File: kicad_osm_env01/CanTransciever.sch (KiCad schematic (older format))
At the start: 23 parts, among them U8 SN65HVD230

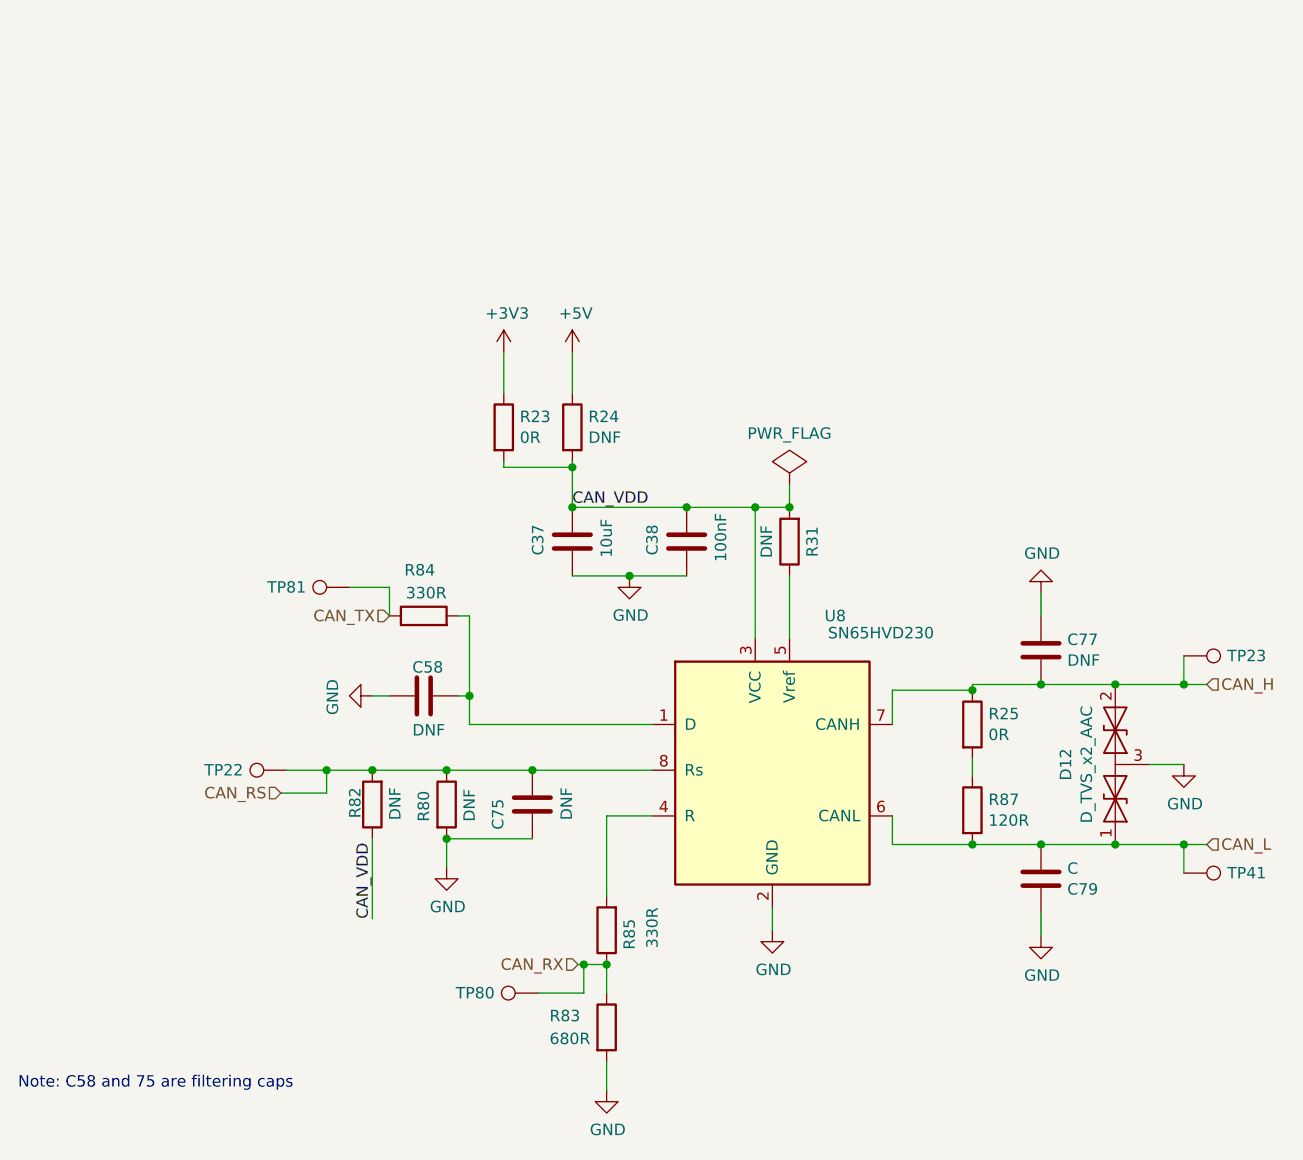
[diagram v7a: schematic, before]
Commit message: updated schematics
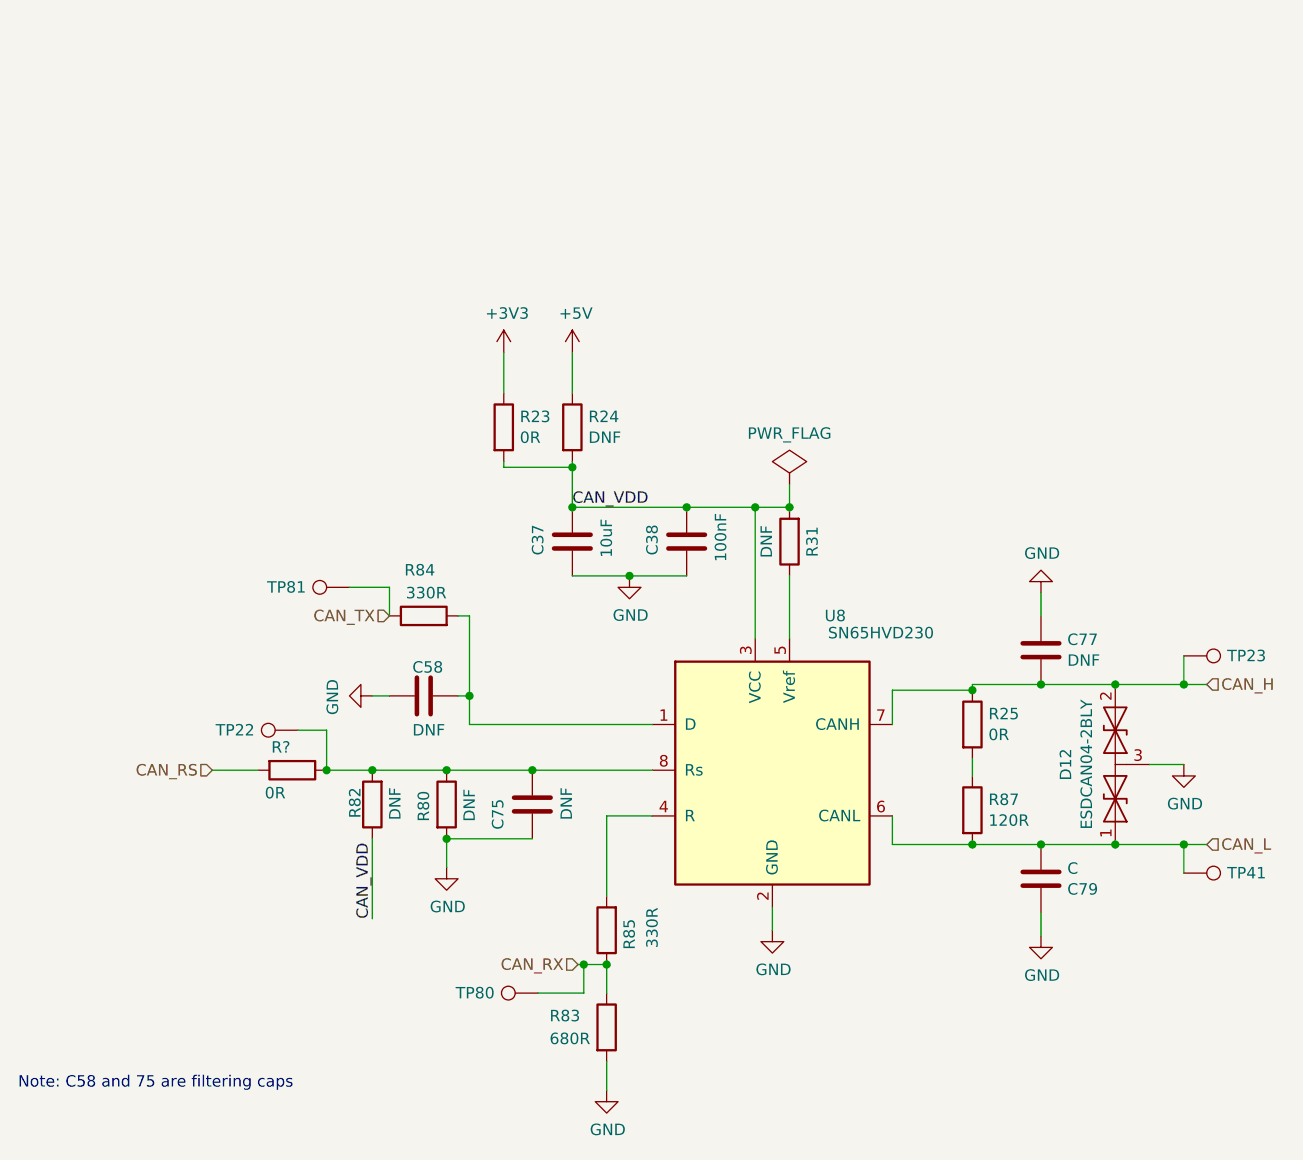
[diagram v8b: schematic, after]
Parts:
- added R?: 0R, symbol device:R
- D12: value D_TVS_x2_AAC -> ESDCAN04-2BLY
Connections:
- net CAN_RS: now also R?.2; no longer C75.2, R80.1, R82.2, TP22.1, U8.8 (Rs)
- new net: C75.2, R80.1, R82.2, R?.1, TP22.1, U8.8 (Rs)
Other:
- moved on the sheet: TP22
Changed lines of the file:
@@
 $Descr A4 11693 8268
 encoding utf-8
-Sheet 11 9
+Sheet 9 9
 Title ""
 Date ""
@@
 Wire Wire Line
 	6900 4025 6900 3950
-Text HLabel 3875 4100 0    50   Input ~ 0
+Text HLabel 3575 4000 0    50   Input ~ 0
 CAN_RS
 $Comp
 L OSM_env01-rescue:Test_Point-Connector-ESP32-EVB_Rev_D-rescue TP?
 U 1 1 61C968D6
-P 3900 4000
+P 3950 3825
 AR Path="/60688D25/61C968D6" Ref="TP?"  Part="1"
 AR Path="/6064BC1D/61C968D6" Ref="TP22"  Part="1"
-F 0 "TP22" V 3900 4275 50  0000 C CNN
-F 1 "Test_Point" V 4004 4072 50  0001 C CNN
-F 2 "TestPoint:TestPoint_Pad_D1.5mm" H 4100 4000 50  0001 C CNN
-F 3 "~" H 4100 4000 50  0001 C CNN
-	1    3900 4000
+F 0 "TP22" V 3950 4100 50  0000 C CNN
+F 1 "Test_Point" V 4054 3897 50  0001 C CNN
+F 2 "TestPoint:TestPoint_Pad_D1.5mm" H 4150 3825 50  0001 C CNN
+F 3 "~" H 4150 3825 50  0001 C CNN
+	1    3950 3825
 	0    -1   1    0
 $EndComp
 Wire Wire Line
-	3900 4000 4075 4000
-Wire Wire Line
-	3875 4100 4075 4100
+	3950 3825 4075 3825
 $Comp
 L OSM_env01-rescue:Test_Point-Connector-ESP32-EVB_Rev_D-rescue TP?
@@
 Wire Wire Line
 	4700 3325 4700 3675
-Connection ~ 4075 4000
-Wire Wire Line
-	4075 4100 4075 4000
 Wire Wire Line
 	5500 3800 4700 3800
@@
 P 7525 3975
 F 0 "D12" H 7525 4191 50  0000 C CNN
-F 1 "D_TVS_x2_AAC" H 7525 4100 50  0000 C CNN
+F 1 "ESDCAN04-2BLY " H 7525 4100 50  0000 C CNN
 F 2 "Package_TO_SOT_SMD:SOT-23" H 7375 3975 50  0001 C CNN
 F 3 "https://en.wikipedia.org/wiki/Transient-voltage-suppression_diode" H 7375 3975 50  0001 C CNN
@@
 Wire Wire Line
 	7675 3975 7825 3975
+$Comp
+L device:R R?
+U 1 1 614A8ACA
+P 3925 4000
+F 0 "R?" V 3825 3950 50  0000 C CNN
+F 1 "0R" V 4025 3925 50  0000 C CNN
+F 2 "" V 3855 4000 50  0001 C CNN
+F 3 "" H 3925 4000 50  0001 C CNN
+	1    3925 4000
+	0    1    1    0
+$EndComp
+Connection ~ 4075 4000
+Wire Wire Line
+	4075 4000 4075 3825
+Wire Wire Line
+	3575 4000 3775 4000
 $EndSCHEMATC
